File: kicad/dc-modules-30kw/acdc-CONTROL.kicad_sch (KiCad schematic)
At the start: 29 parts

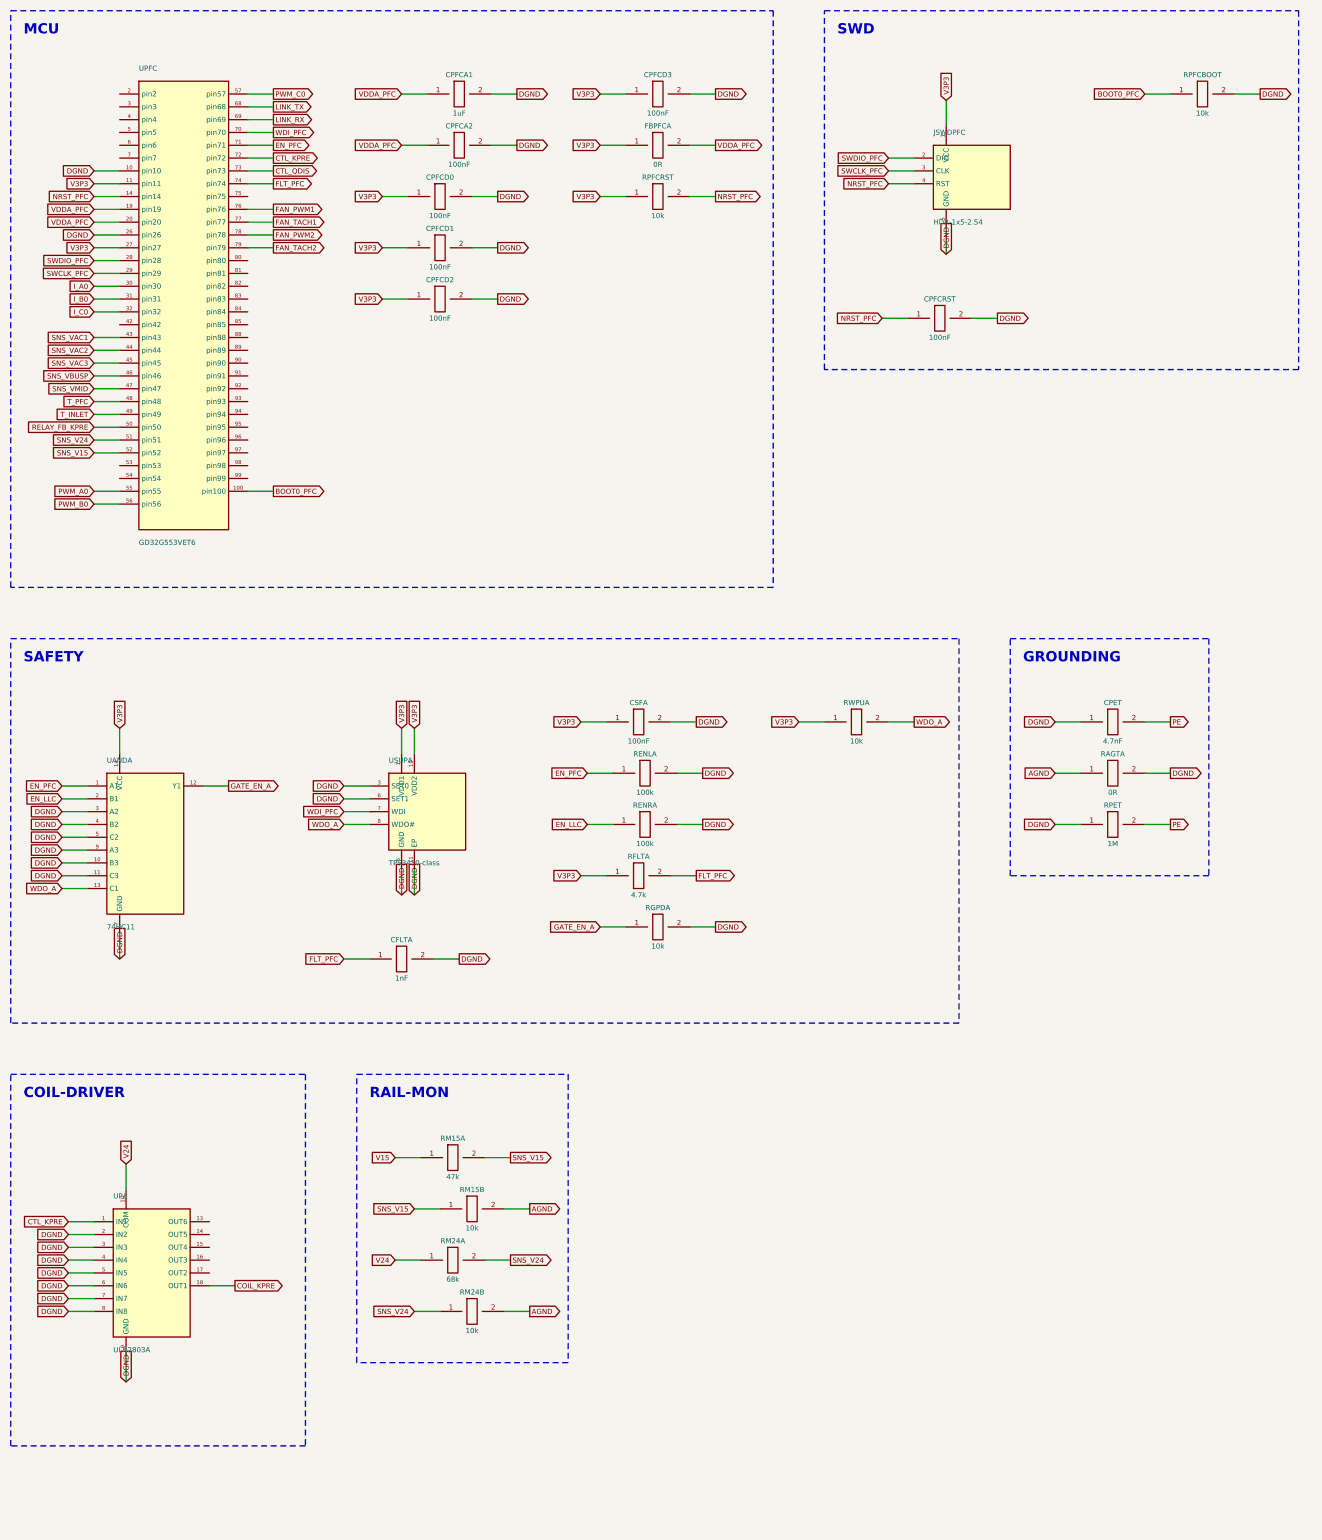
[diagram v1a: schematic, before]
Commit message: Rebuild the GD32G553VET6 pin map against the datasheet
The map was STM32G474-derived and headed pin(symbolic); gate item A6 had
recorded the GD32G553 check as pending and it was never closed. It put the
fault output on pin 74 (VSS) and BOOT0 on pin 100 (VDD) -- two hard shorts
-- and SWD on PA6/PA7, so the part was also unprogrammable as drawn.

Allocated against GD32G553xx Rev 2.0 Table 2-4 for the 120 kW worst case
(59 PFC / 80 LLC signals on 100 pins), then adversarially audited. The audit
caught a safety-critical error in the first LLC pass: PA6 cannot be
TIMER0_BRKIN0 and TIMER7_BRKIN0 at once (AF6 vs AF4, one AFSEL per pin),
which would have left four legs -- eight switches at 120 kW -- with no
hardware fault shutdown. FLT_LLC now lands on three pins, one per advanced
timer. VBAT is tied to V3P3 only; grounding it would unpower the backup
domain and kill PC13, which now carries one of those break inputs.

Applied through the remap, so the emitted netlists carry real package pins:
BOOT0 95, SWDIO 76, SWCLK 77, VDDA 37, VSSA 35, VREFP 36, all five VDD/VSS
pairs populated. Both verifiers still 100.00% (1735/1735 pins, 608
components); all review checks pass.

Four architecture decisions are documented as open rather than defaulted:
HRTIMER-vs-advanced-timer for the LLC (HRTIMER has 16 outputs, the LLC needs
24), the PFC ADC interleave scheme, LLC fan channels, and IOUT differential
mode. The map is correct and can no longer short a rail, but is not frozen.

Co-Authored-By: Claude Fable 5 <noreply@anthropic.com>
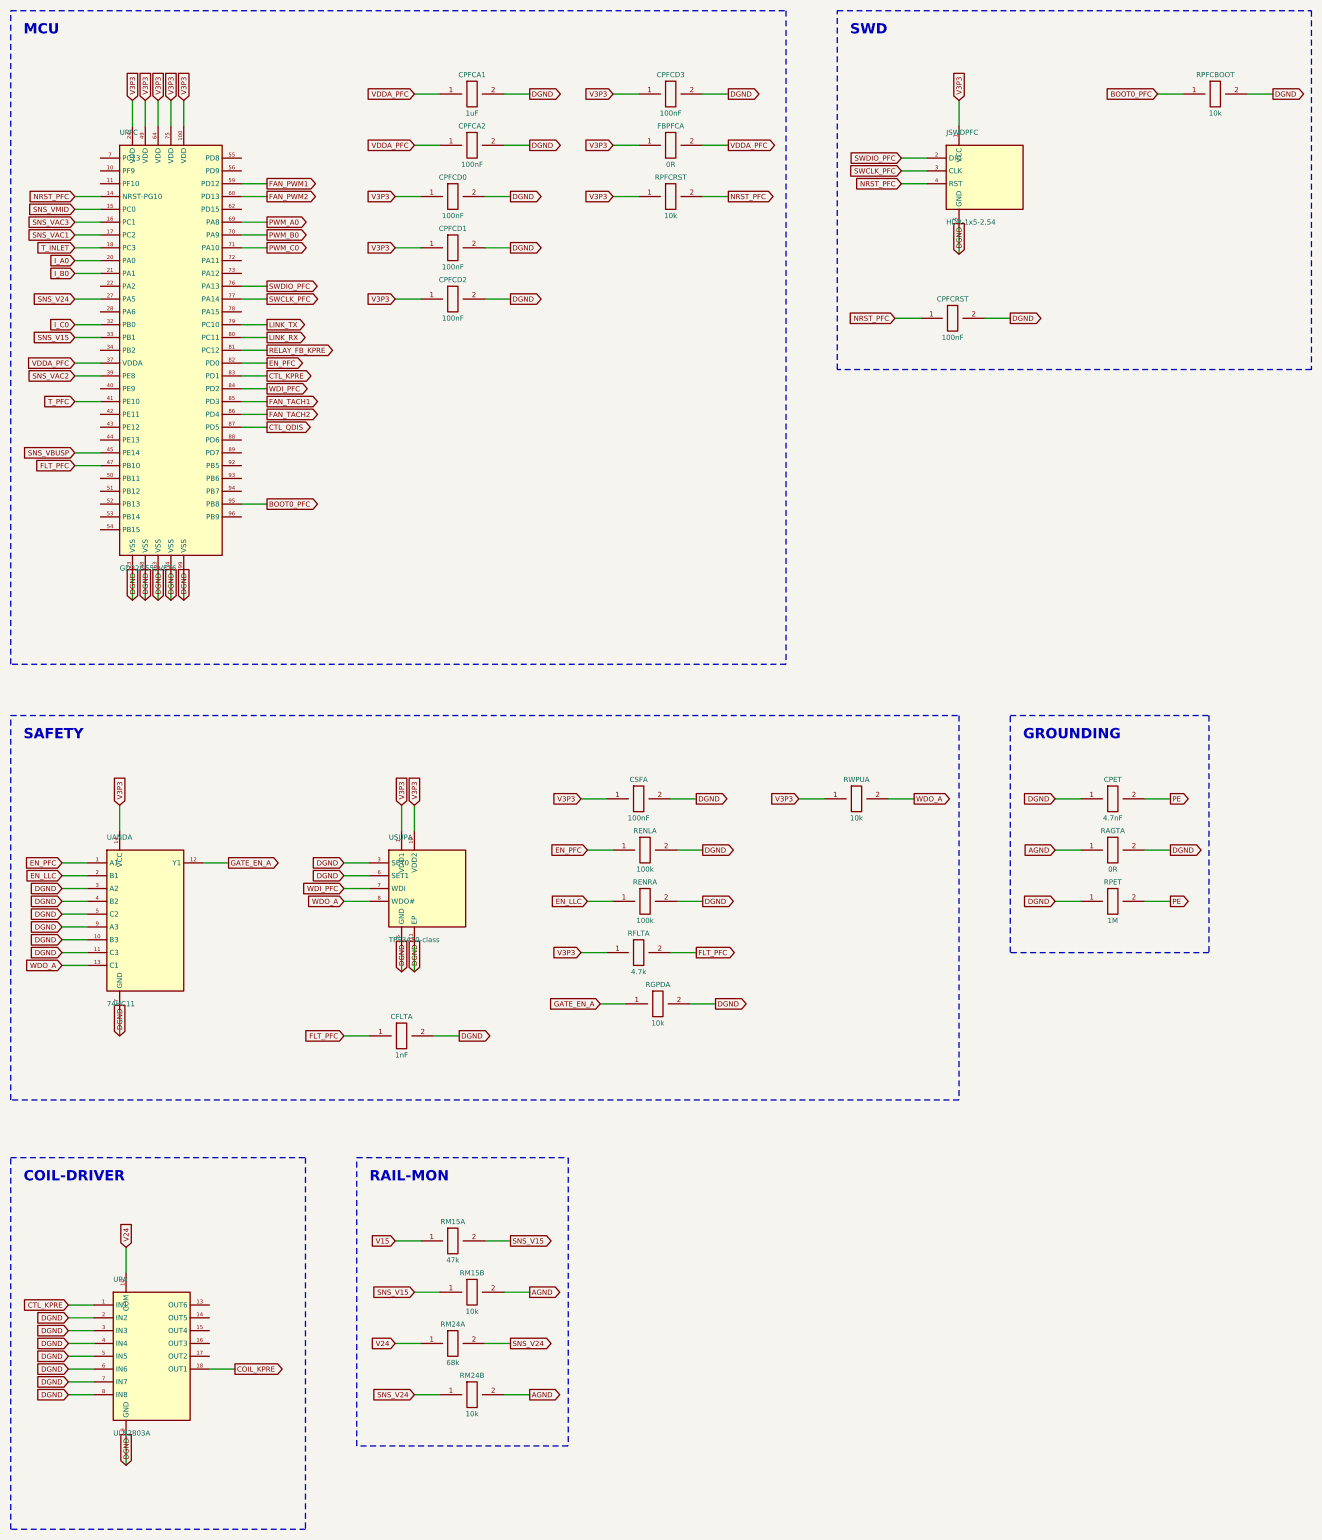
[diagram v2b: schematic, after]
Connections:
- net BOOT0_PFC: now also UPFC.95 (PB8); no longer UPFC.100 (pin100)
- net CTL_KPRE: now also UPFC.83 (PD1); no longer UPFC.72 (pin72)
- net CTL_QDIS: now also UPFC.87 (PD5); no longer UPFC.73 (pin73)
- net DGND: now also UPFC.23 (VSS), UPFC.48 (VSS), UPFC.63 (VSS), UPFC.74 (VSS), UPFC.99 (VSS); no longer UPFC.10 (pin10), UPFC.26 (pin26)
- net EN_PFC: now also UPFC.82 (PD0); no longer UPFC.71 (pin71)
- net FAN_PWM1: now also UPFC.59 (PD12); no longer UPFC.76 (pin76)
- net FAN_PWM2: now also UPFC.60 (PD13); no longer UPFC.78 (pin78)
- net FAN_TACH1: now also UPFC.85 (PD3); no longer UPFC.77 (pin77)
- net FAN_TACH2: now also UPFC.86 (PD4); no longer UPFC.79 (pin79)
- net FLT_PFC: now also UPFC.47 (PB10); no longer UPFC.74 (pin74)
- net I_A0: now also UPFC.20 (PA0); no longer UPFC.30 (pin30)
- net I_B0: now also UPFC.21 (PA1); no longer UPFC.31 (pin31)
- net LINK_RX: now also UPFC.80 (PC11); no longer UPFC.69 (pin69)
- net LINK_TX: now also UPFC.79 (PC10); no longer UPFC.68 (pin68)
- net PWM_A0: now also UPFC.69 (PA8); no longer UPFC.55 (pin55)
- net PWM_B0: now also UPFC.70 (PA9); no longer UPFC.56 (pin56)
- net PWM_C0: now also UPFC.71 (PA10); no longer UPFC.57 (pin57)
- net RELAY_FB_KPRE: now also UPFC.81 (PC12); no longer UPFC.50 (pin50)
- net SNS_V15: now also UPFC.33 (PB1); no longer UPFC.52 (pin52)
- net SNS_V24: now also UPFC.27 (PA5); no longer UPFC.51 (pin51)
- net SNS_VAC1: now also UPFC.17 (PC2); no longer UPFC.43 (pin43)
- net SNS_VAC2: now also UPFC.39 (PE8); no longer UPFC.44 (pin44)
- net SNS_VAC3: now also UPFC.16 (PC1); no longer UPFC.45 (pin45)
- net SNS_VBUSP: now also UPFC.45 (PE14); no longer UPFC.46 (pin46)
- net SNS_VMID: now also UPFC.15 (PC0); no longer UPFC.47 (pin47)
- net SWCLK_PFC: now also UPFC.77 (PA14); no longer UPFC.29 (pin29)
- net SWDIO_PFC: now also UPFC.76 (PA13); no longer UPFC.28 (pin28)
- net T_INLET: now also UPFC.18 (PC3); no longer UPFC.49 (pin49)
- net T_PFC: now also UPFC.41 (PE10); no longer UPFC.48 (pin48)
- net V3P3: now also UPFC.100 (VDD), UPFC.24 (VDD), UPFC.49 (VDD), UPFC.64 (VDD), UPFC.75 (VDD); no longer UPFC.11 (pin11), UPFC.27 (pin27)
- net VDDA_PFC: now also UPFC.37 (VDDA); no longer UPFC.19 (pin19), UPFC.20 (pin20)
- net WDI_PFC: now also UPFC.84 (PD2); no longer UPFC.70 (pin70)
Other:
- moved on the sheet: CFLTA, CPET, CPFCA1, CPFCA2, CPFCD0, CPFCD1, CPFCD2, CPFCD3, CPFCRST, CSFA, FBPFCA, JSWDPFC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
